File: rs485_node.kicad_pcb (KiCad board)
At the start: 2 copper layers, 8 parts, among them J2 Conn_01x04_Male, U1 SHT30-DIS, U2 ATtiny214-SS, U3 ST485EBDR

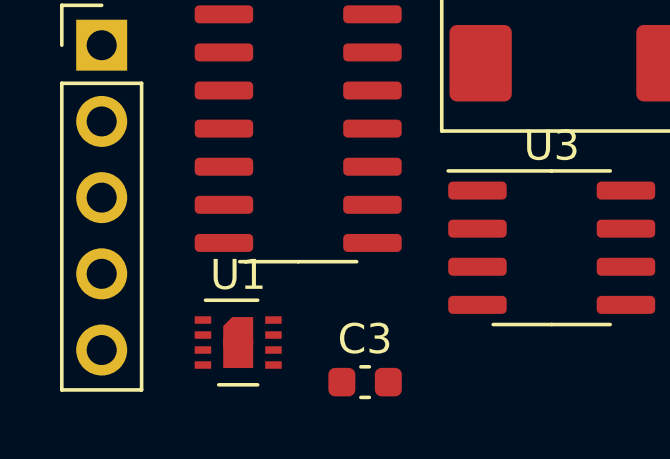
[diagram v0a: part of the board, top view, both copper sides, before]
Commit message: Change to SHT40
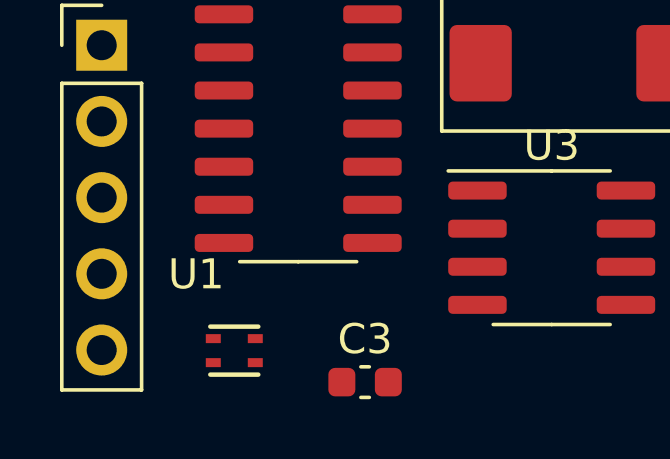
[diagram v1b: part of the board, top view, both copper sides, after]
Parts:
- U1: value SHT30-DIS -> SHT40; footprint Sensor_Humidity:Sensirion_DFN-8-1EP_2.5x2.5mm_P0.5mm_EP1.1x1.7mm -> SHT40:SHT40
- moved U1 0.30 mm to (151.5, 94.8)
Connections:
- U1 pad 3: Net-(U1-Pad3) -> (no net)
- U1 pad 4: Net-(U1-Pad4) -> Net-(C1-Pad1)
- U2 pad 9: Net-(U1-Pad4) -> Net-(U1-Pad2)

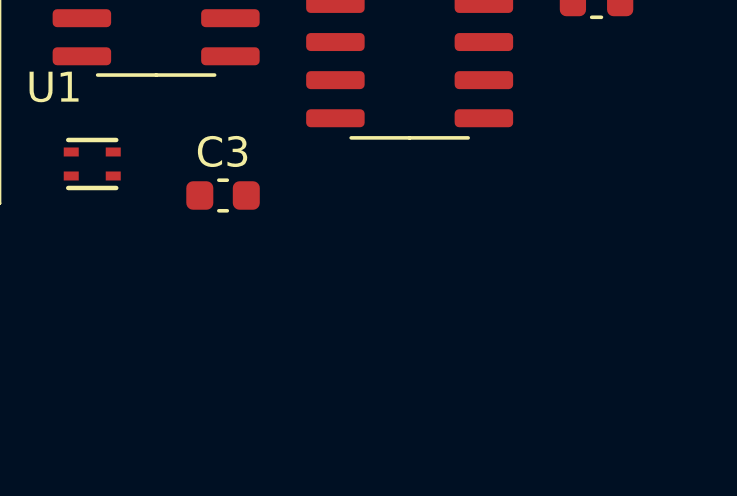
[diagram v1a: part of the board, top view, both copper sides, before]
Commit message: Added 3V3 LDO
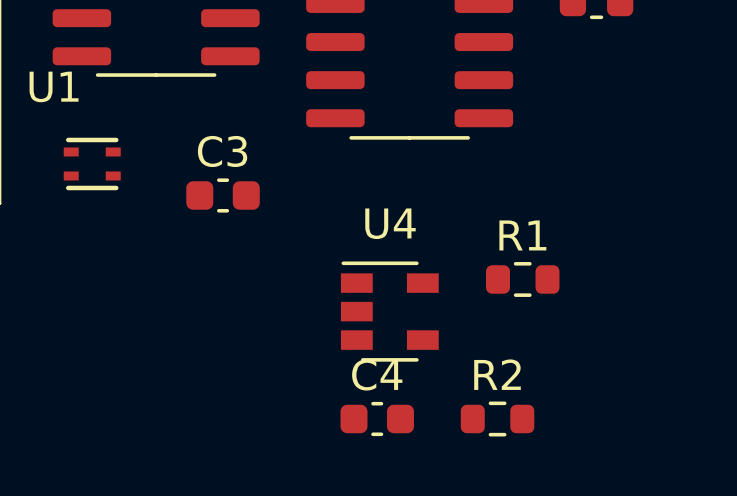
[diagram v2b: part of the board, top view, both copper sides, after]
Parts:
- added C4: 1n, Capacitor_SMD:C_0603_1608Metric, F.Cu at (161.0, 103.2)
- added R1: R, Resistor_SMD:R_0603_1608Metric, F.Cu at (165.8, 98.6)
- added R2: R, Resistor_SMD:R_0603_1608Metric, F.Cu at (165.0, 103.2)
- added U4: MIC5504-3.3YM5, Package_TO_SOT_SMD:SOT-23-5, F.Cu at (161.4, 99.7)
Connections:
- C2 pad 1: Net-(C1-Pad1) -> Net-(C2-Pad1)
- C3 pad 1: Net-(C1-Pad1) -> Net-(C2-Pad1)
- FB1 pad 2: Net-(C1-Pad1) -> Net-(C2-Pad1)
- U2 pad 12: Net-(U2-Pad12) -> Net-(R1-Pad1)
- U3 pad 1: Net-(U2-Pad12) -> Net-(R2-Pad1)
- U3 pad 8: Net-(C1-Pad1) -> Net-(C2-Pad1)

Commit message: CM filter, termination etc.
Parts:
- added C10: 1n, Capacitor_SMD:C_0603_1608Metric, F.Cu at (181.2, 63.5)
- added C11: 1n, Capacitor_SMD:C_0603_1608Metric, F.Cu at (181.2, 67.2)
- added C12: 100n, Capacitor_SMD:C_0603_1608Metric, F.Cu at (167.8, 62.2)
- added C13: 100n, Capacitor_SMD:C_0603_1608Metric, F.Cu at (175.8, 61.5)
- added C5: 10n, Capacitor_SMD:C_0603_1608Metric, F.Cu at (144.5, 64.0)
- added C6: 10n, Capacitor_SMD:C_0603_1608Metric, F.Cu at (144.5, 61.5)
- added C7: 10n, Capacitor_SMD:C_0603_1608Metric, F.Cu at (144.5, 59.0)
- added C8: 10n, Capacitor_SMD:C_0603_1608Metric, F.Cu at (144.5, 69.2)
- added C9: 10n, Capacitor_SMD:C_0603_1608Metric, F.Cu at (144.5, 66.5)
- added D1: LED, LED_SMD:LED_0805_2012Metric, F.Cu at (140.8, 56.0)
- added FL1: WE-SL2, rs485_node:WE-SL2, F.Cu at (175.0, 65.8)
- added J1: Conn_01x03_Male, Connector_PinHeader_2.54mm:PinHeader_1x03_P2.54mm_Vertical, F.Cu at (156.2, 56.5)
- added J3: Conn_01x06_Male, Connector_PinHeader_2.54mm:PinHeader_1x06_P2.54mm_Vertical, F.Cu at (136.7, 56.3)
- added JP1: SolderJumper_2_Open, Jumper:SolderJumper-2_P1.3mm_Open_RoundedPad1.0x1.5mm, B.Cu at (151.8, 61.2)
- added JP2: SolderJumper_2_Open, Jumper:SolderJumper-2_P1.3mm_Open_RoundedPad1.0x1.5mm, B.Cu at (151.8, 63.8)
- added JP3: SolderJumper_2_Open, Jumper:SolderJumper-2_P1.3mm_Open_RoundedPad1.0x1.5mm, B.Cu at (151.8, 66.2)
- added R3: R, Resistor_SMD:R_0603_1608Metric, F.Cu at (144.5, 56.0)
- added R4: R, Resistor_SMD:R_0603_1608Metric, F.Cu at (140.5, 59.0)
- added R5: R, Resistor_SMD:R_0603_1608Metric, F.Cu at (140.5, 61.5)
- added R6: R, Resistor_SMD:R_0603_1608Metric, F.Cu at (140.5, 64.0)
- added R7: R, Resistor_SMD:R_0603_1608Metric, F.Cu at (140.5, 69.2)
- added R8: R, Resistor_SMD:R_0603_1608Metric, F.Cu at (140.5, 66.5)
- added R9: R, Resistor_SMD:R_0603_1608Metric, F.Cu at (172.5, 61.5)
- added SW1: SW_DIP_x03, Package_DIP:SMDIP-6_W7.62mm, B.Cu at (152.8, 63.8)
- C3: value 1n -> 10n
- C4: value 1n -> 1u
- FB1: value Ferrite_Bead_Small -> 1000R@100
- J2: footprint Connector_PinHeader_2.54mm:PinHeader_1x05_P2.54mm_Vertical -> Connector_PinHeader_2.54mm:PinHeader_1x04_P2.54mm_Vertical
- U1: footprint SHT40:SHT40 -> rs485_node:SHT40
- moved C4 46.5 mm to (162.2, 56.7), turned to 90 degrees
- moved C3 46.4 mm to (181.0, 56.8), turned to 90 degrees
- moved J2 45.2 mm to (184.0, 58.5)
- moved U4 42.7 mm to (166.0, 57.2), turned to 180 degrees
- moved R2 41.8 mm to (163.0, 61.5), turned to 90 degrees
- moved R1 39.0 mm to (160.2, 60.0), turned to 90 degrees
- moved FB1 34.3 mm to (179.0, 56.7), turned to 90 degrees
- moved C1 31.5 mm to (148.5, 60.2), turned to 180 degrees
- moved C2 29.3 mm to (173.2, 57.8)
- moved U1 24.9 mm to (153.8, 70.0)
- moved U3 24.8 mm to (165.5, 66.8)
- moved U2 23.4 mm to (154.0, 64.0)
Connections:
- C2 pad 1: Net-(C2-Pad1) -> Net-(C12-Pad1)
- C3 pad 1: Net-(C2-Pad1) -> Net-(C3-Pad1)
- FB1 pad 1: Net-(FB1-Pad1) -> Net-(C3-Pad1)
- FB1 pad 2: Net-(C2-Pad1) -> Net-(C12-Pad1)
- J2 pad 2: Net-(FB1-Pad1) -> Net-(C3-Pad1)
- U1 pad 3: (no net) -> GND
- U3 pad 8: Net-(C2-Pad1) -> Net-(C12-Pad1)
- U4 pad 1: Net-(C2-Pad1) -> Net-(C12-Pad1)
- U4 pad 3: Net-(C2-Pad1) -> Net-(C12-Pad1)
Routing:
- net Net-(J1-Pad3): track 0.00 -> 45.1 mm, vias 0 -> 1
- net Net-(C12-Pad1): track 0.00 -> 44.6 mm
- net Net-(C1-Pad1): track 0.00 -> 32.7 mm, vias 0 -> 2
- net GND: track 0.00 -> 28.4 mm, vias 0 -> 16
- net Net-(C8-Pad1): track 0.00 -> 25.1 mm
- net Net-(JP1-Pad1): track 0.00 -> 20.0 mm, vias 0 -> 1
- net Net-(C9-Pad1): track 0.00 -> 17.9 mm
- net Net-(C7-Pad1): track 0.00 -> 17.1 mm
- net Net-(U2-Pad2): track 0.00 -> 16.0 mm
- net Net-(C3-Pad1): track 0.00 -> 13.9 mm
- net Net-(C13-Pad2): track 0.00 -> 13.2 mm
- net Net-(C6-Pad1): track 0.00 -> 11.8 mm
- net Net-(C5-Pad1): track 0.00 -> 11.2 mm
- net Net-(JP2-Pad1): track 0.00 -> 9.83 mm, vias 0 -> 1
- net Net-(U2-Pad11): track 0.00 -> 9.50 mm
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- added copper zone on B.Cu, net GND
- added copper zone on F.Cu, net GND
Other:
- board outline added: 53 x 18 mm
